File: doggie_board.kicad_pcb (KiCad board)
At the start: 4 copper layers, 127 x 127 mm, 110 parts, among them J1 Conn_01x03, J2 XT90PW-M, J3 XT90PW-M, J4 Conn_01x02, J5 Conn_01x03, J5V1 48v, J5V10 48v, J5V11 48v, J5V12 48v, J5V13 12v, J5V14 12v, J5V15 12v, J5V16 12v, J5V17 3.3v, J5V18 3.3v, J5V19 3.3v, J5V2 48v, J5V20 3.3v, J5V21 5v, J5V22 5v, J5V23 5v, J5V24 5v, J5V3 48v, J5V4 48v, J5V5 48v, J5V6 48v, J5V7 48v, J5V8 48v, J5V9 48v, J6 Conn_01x02, J7 Conn_01x03, J8 Conn_01x03, Q1 PSMN3R7-100BSEJ, Q10 2N7002, Q11 2N7002, Q12 2N7002, Q2 PSMN3R7-100BSEJ, Q3 PSMN3R7-100BSEJ, Q4 PSMN3R7-100BSEJ, Q5 PSMN3R7-100BSEJ, Q6 PSMN3R7-100BSEJ, Q7 Q_NMOS, Q8 Q_NMOS, Q9 2N7002, SW1 SW_SPST, U1 TPS2490, U2 LM5148RGYR, U3 TPS566242DRLR, U4 TPS566242DRLR

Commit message: added my name
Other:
- board text added: "Made by: Niranjan Mathirajan, Siddharth Vasudevan, Alperen Ozpolat"
- board text added: "UMass Robotics - Doggie Power"

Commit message: om suggestions
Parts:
- J5V13, J5V21: footprint Connector_BarrelJack:BarrelJack_CUI_PJ-079BH_Horizontal -> footprints:CUI_PJ-037A
- R1: value 300k -> 120k
- R4: value 18k -> 240k
- moved J5V13 6.71 mm to (63.8, 151.6), turned to -90 degrees
- moved J5V21 4.53 mm to (80.2, 151.4), turned to -90 degrees
- moved J5 3.60 mm to (114.2, 158.5)
- moved J7 3.60 mm to (117.8, 158.5)
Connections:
- net Net-(Q7-D) renamed /12v Buck Converter/switch 12v
- net Net-(Q7-G) renamed /12v Buck Converter/low_fet
- net Net-(Q8-G) renamed /12v Buck Converter/high_fet
- net Net-(U2-ISNS+) renamed /12v Buck Converter/sense
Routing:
- net +12V: track 148.9 -> 130.4 mm
- net /12v Buck Converter/switch 12v: track 23.9 -> 11.9 mm
- net +5V: track 51.8 -> 43.2 mm
- net /12v Buck Converter/sense: track 15.9 -> 9.48 mm
- net /5v Buck Converter/5V_EN: track 7.10 -> 11.6 mm
- net +5V_LP: track 13.1 -> 9.94 mm
- net 48_RAW: track 149.9 -> 148.4 mm
- net +3.3V: track 32.9 -> 33.9 mm
- net /3.3v Buck Converter/SW: track 11.2 -> 12.0 mm
- added copper zone on F.Cu, net /12v Buck Converter/sense
- added copper zone on F.Cu, net /12v Buck Converter/switch 12v

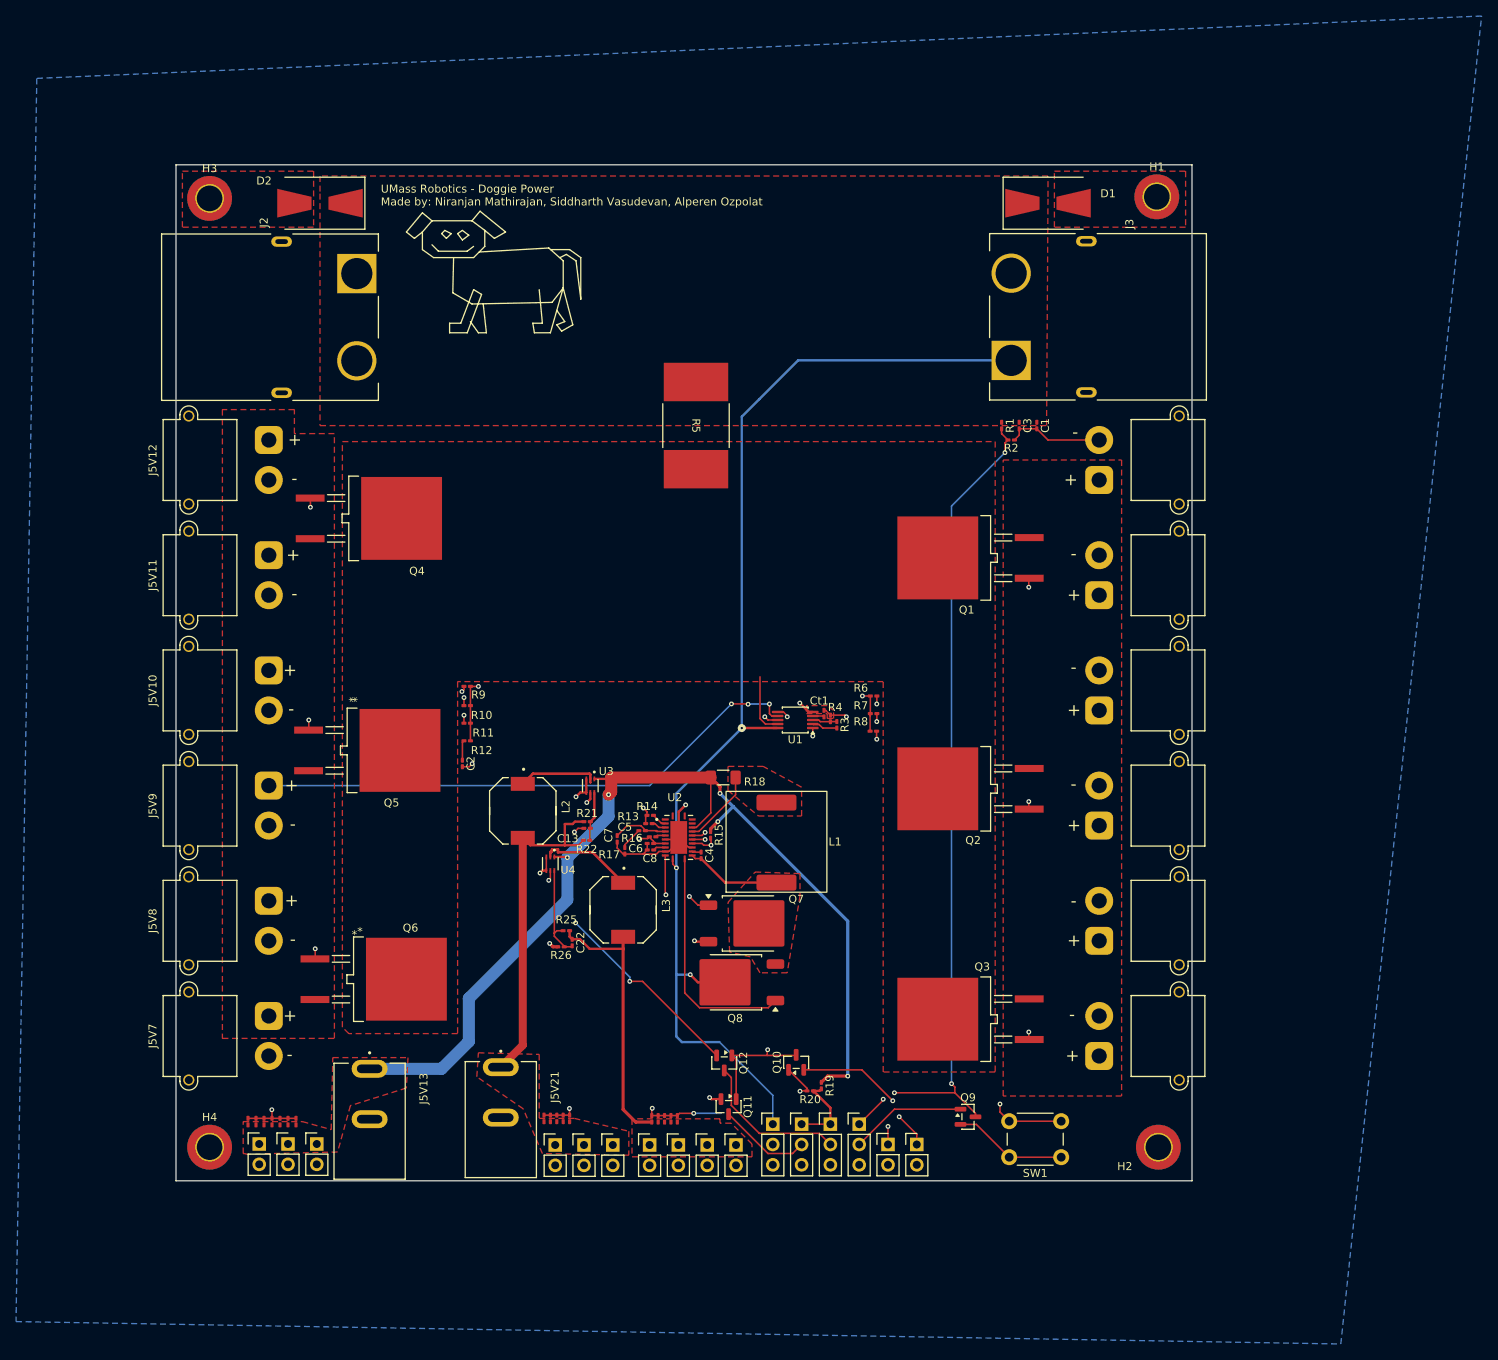
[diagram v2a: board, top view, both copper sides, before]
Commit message: shortened board
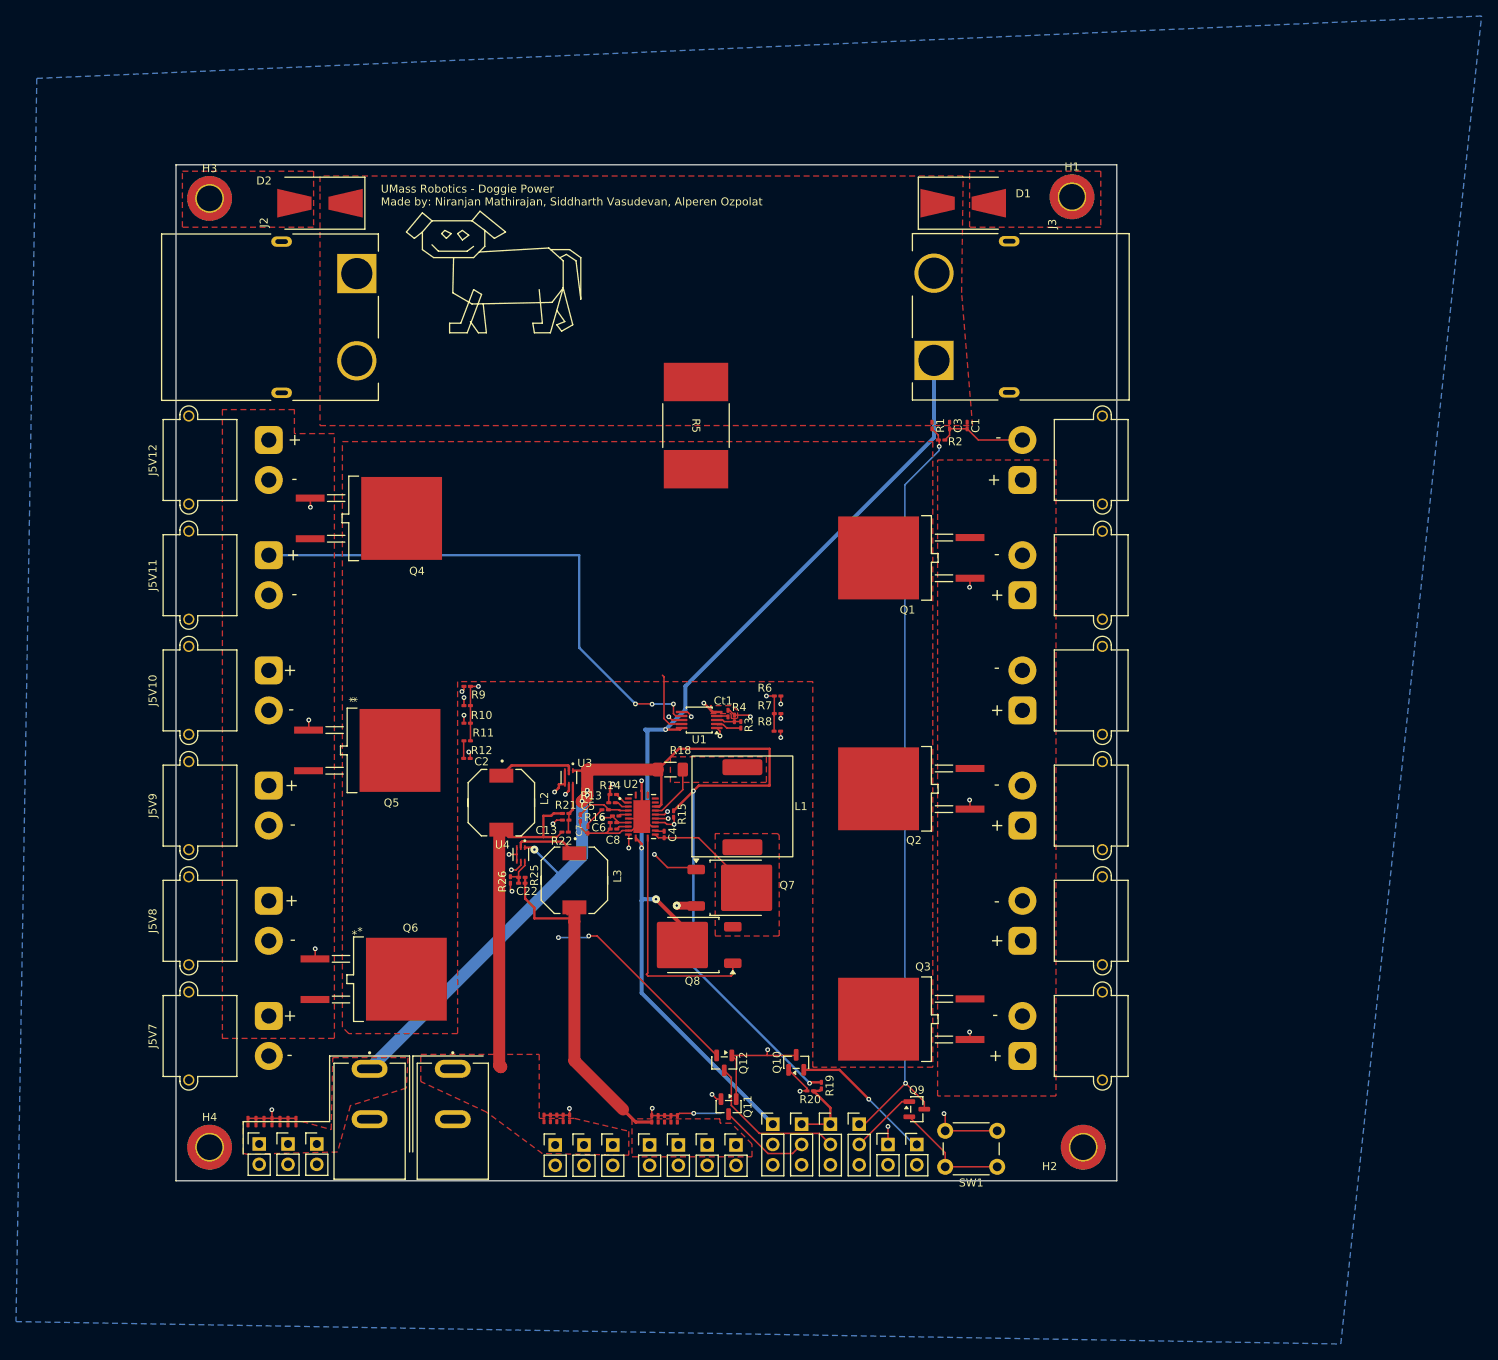
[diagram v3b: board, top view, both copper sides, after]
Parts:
- moved Ct1 12.0 mm to (108.6, 107.2)
- moved R3 12.0 mm to (110.2, 108.6)
- moved R4 12.0 mm to (109.4, 107.8)
- moved R6 12.0 mm to (114.8, 105.0)
- moved R7 12.0 mm to (114.8, 107.2)
- moved R8 12.0 mm to (114.8, 109.4)
- moved U1 12.0 mm to (105.0, 108.0)
- moved D1 10.6 mm to (138.0, 43.4)
- moved H1 10.6 mm to (151.6, 42.6)
- moved R26 10.5 mm to (81.4, 128.0), turned to -90 degrees
- moved C22 9.73 mm to (82.8, 128.4), turned to 180 degrees
- moved J3 9.65 mm to (143.8, 57.6)
- moved J5V1 9.60 mm to (145.4, 78.0)
- moved J5V2 9.60 mm to (145.4, 92.4)
- moved J5V3 9.60 mm to (145.4, 106.8)
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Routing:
- net +12V: track 130.4 -> 150.4 mm, vias 5 -> 6
- net 48_RAW: track 148.4 -> 133.3 mm
- net +48V: track 110.7 -> 123.1 mm
- net +3.3V: track 33.9 -> 44.1 mm
- net Net-(Q1-Pad1): track 27.2 -> 36.1 mm
- net /High Side Power Switch/sw_low: track 104.1 -> 96.3 mm, vias 4 -> 2
- net Net-(U4-FB): track 12.3 -> 4.86 mm
- net Net-(Q12-S): track 32.8 -> 38.9 mm
- net Net-(J1-Pin_2): track 14.5 -> 8.48 mm
- net 12V_PG: track 46.3 -> 52.0 mm
- net 48V_PG: track 60.2 -> 65.2 mm
- net /12v Buck Converter/12V_EN: track 45.4 -> 50.0 mm
- net Net-(Q2-Pad1): track 25.1 -> 29.6 mm
- net /3.3v Buck Converter/SW: track 12.0 -> 7.97 mm
- net ps_sw: track 65.8 -> 68.7 mm
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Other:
- board size 127 x 127 mm -> 117.6 x 127 mm

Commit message: fixed clearances
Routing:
- net 48_RAW: track 133.3 -> 132.7 mm
- net +48V: vias 3 -> 1
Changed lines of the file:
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@@
 			(pintype "passive")
 			(solder_mask_margin 0.102)
+			(clearance 1)
 		)
 		(pad "P" thru_hole rect
@@
 			(pinfunction "Pin_2")
 			(pintype "passive")
+			(clearance 0.7)
 		)
 		(embedded_fonts no)
@@
 			(pinfunction "Pin_2")
 			(pintype "passive")
+			(clearance 0.7)
 		)
 		(embedded_fonts no)
@@
 			(pintype "passive")
 			(solder_mask_margin 0.102)
+			(clearance 1)
 		)
 		(pad "P" thru_hole rect
@@
 			(pinfunction "Pin_2")
 			(pintype "passive")
+			(clearance 0.7)
 		)
 		(embedded_fonts no)
@@
 			(pinfunction "Pin_2")
 			(pintype "passive")
+			(clearance 0.7)
 		)
 		(embedded_fonts no)
@@
 			(pinfunction "Pin_2")
 			(pintype "passive")
+			(clearance 0.7)
 		)
 		(embedded_fonts no)
@@
 			(pinfunction "Pin_2")
 			(pintype "passive")
+			(clearance 0.7)
 		)
 		(embedded_fonts no)
@@
 			(pinfunction "Pin_2")
 			(pintype "passive")
+			(clearance 0.7)
 		)
 		(embedded_fonts no)
@@
 			(pinfunction "Pin_2")
 			(pintype "passive")
+			(clearance 0.7)
 		)
 		(embedded_fonts no)
@@
 			(pinfunction "Pin_2")
 			(pintype "passive")
+			(clearance 0.7)
 		)
 		(embedded_fonts no)
@@
 			(pinfunction "Pin_2")
 			(pintype "passive")
+			(clearance 0.7)
 		)
 		(embedded_fonts no)
@@
 	)
 	(segment
+		(start 98.531 109.476099)
+		(end 100.523901 109.476099)
+		(width 0.5)
+		(layer "B.Cu")
+		(net 2)
+	)
+	(segment
 		(start 98.531 120.923901)
 		(end 97.8 121.654901)
@@
 	)
 	(segment
-		(start 97.8 130.6)
-		(end 97.8 142.12)
+		(start 100.523901 109.476099)
+		(end 100.8 109.2)
 		(width 0.5)
 		(layer "B.Cu")
@@
 	)
 	(segment
-		(start 99.6 130.4)
-		(end 98 130.4)
+		(start 97.8 130.6)
+		(end 97.8 142.12)
 		(width 0.5)
 		(layer "B.Cu")
@@
 	)
 	(segment
-		(start 100.8 109.2)
-		(end 98.254901 109.2)
+		(start 99.6 130.4)
+		(end 98 130.4)
 		(width 0.5)
 		(layer "B.Cu")
@@
 	)
 	(segment
-		(start 98.254901 109.2)
-		(end 98.531 109.476099)
-		(width 0.5)
-		(layer "B.Cu")
-		(net 2)
-	)
-	(segment
 		(start 103.273671 103.776329)
 		(end 103.273671 106.726329)
@@
 		(start 97.0594 158.2594)
 		(end 95.49 156.69)
-		(width 0.4)
+		(width 1.5)
 		(layer "F.Cu")
 		(net 14)
@@
 	)
 	(segment
-		(start 99.11 106.03)
-		(end 99.07 105.99)
-		(width 0.2)
-		(layer "F.Cu")
-		(net 20)
-	)
-	(segment
 		(start 102.069462 107.5)
 		(end 101.78 107.210538)
@@
 		(net 20)
 	)
-	(segment
-		(start 99.07 105.99)
-		(end 97.03 105.99)
-		(width 0.2)
-		(layer "F.Cu")
-		(net 20)
-	)
-	(via
-		(at 97.03 105.99)
-		(size 0.6)
-		(drill 0.3)
-		(layers "F.Cu" "B.Cu")
-		(net 20)
-	)
 	(via
 		(at 101.78 106)
@@
 		(net 20)
 	)
-	(via
-		(at 99.11 106.03)
-		(size 0.6)
-		(drill 0.3)
-		(layers "F.Cu" "B.Cu")
+	(segment
+		(start 99.13 105.99)
+		(end 99.14 106)
+		(width 0.3)
+		(layer "B.Cu")
 		(net 20)
 	)
@@
 		(start 101.78 106)
 		(end 99.14 106)
-		(width 0.2)
+		(width 0.3)
 		(layer "B.Cu")
 		(net 20)
@@
 		(width 0.3)
 		(layer "B.Cu")
+		(net 20)
+	)
+	(segment
+		(start 97.03 105.99)
+		(end 99.13 105.99)
+		(width 0.3)
+		(layer "B.Cu")
